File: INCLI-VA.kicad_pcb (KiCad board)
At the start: 2 copper layers, 100 x 100 mm, 168 parts, among them J1 MSTBV 2,5/5-GF-5,08, J2 MSTBV 2,5/2-GF-5,08, J401 USB4105-GF-A, J402 UART0, Q101 STD18NF25, Q102 IPD30N10S3L-34, Q701 DMN10H220LQ, Q751 DMN10H220LQ, SW401 RESET, SW402 BOOT, U101 LM74930QRGERQ1, U201 LMR38010SQDDARQ1, U301 TPS62A02QDRLRQ1, U302 LP5907QMFX-3.3Q1, U401 ESP32-S3-WROOM-1-N8R2, U402 USBLC6-2SC6, U501 SCL3300-D01, U502 ASM330LHHTR, U503 AS5147U-HTSM, U601 ADM3055E, U701 74AHCT1G126, U751 74AHCT1G126, U801 TPS3828-33Q1

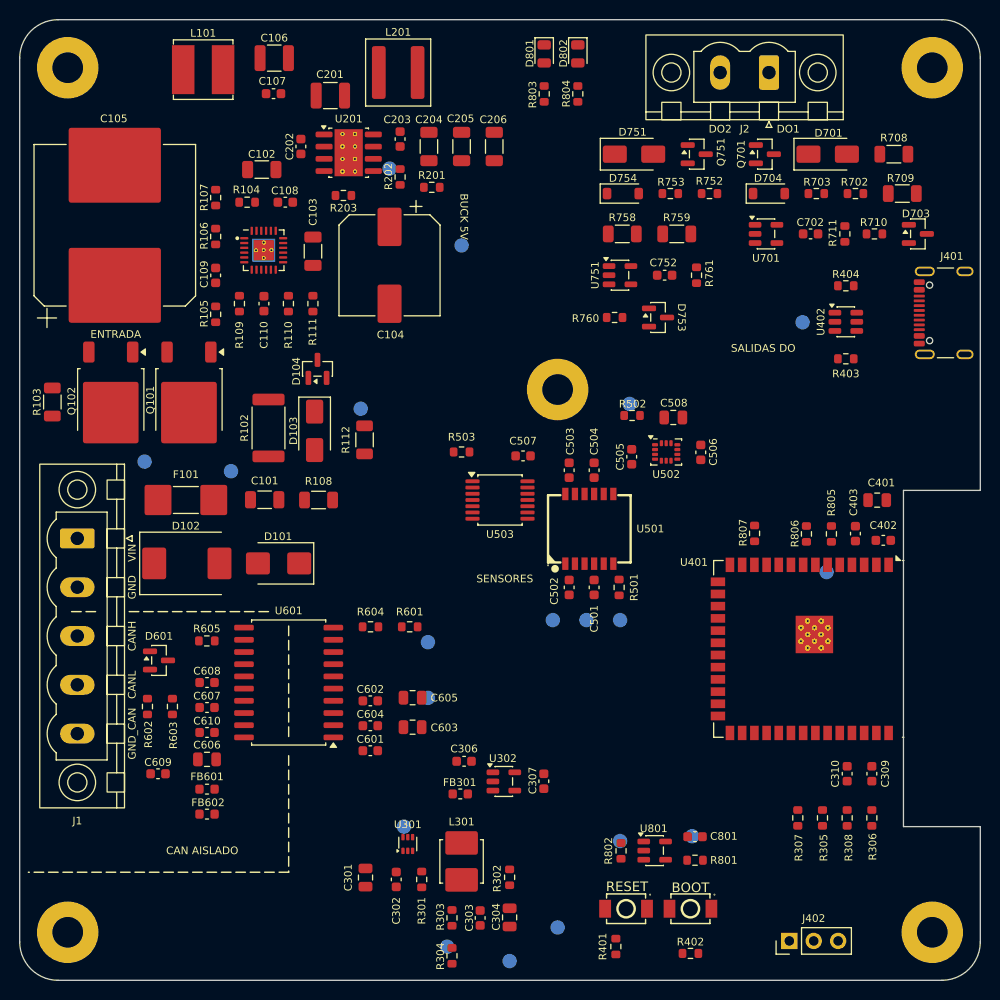
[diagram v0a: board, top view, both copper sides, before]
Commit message: [Claude Code] PCB: placement-v1 - desacoples de U601, lazo del buck, C105 J16 Panasonic y zonas sin barniz
- C601 a 1.1 mm del pin VIO (ADI Rev. D: pista <= 2 mm); C604, C607/C608 reordenados.
- L201 y C203 mas cerca de U201 (SW 2.8 mm, BOOT 1.1 mm).
- C105: huella INCLI-VA:CP_Elec_Panasonic_J16_VibProof (land antivibracion J16, acepta
  EEE-FK1H102AV y EEE-FK1H102AM); MPN PROD EEE-FK1H102AV.
- Coating: zonas a enmascarar en User.Comments y rotulo "SIN BARNIZ".
- PENDIENTES: decisiones del usuario cerradas, requisitos de la caja y plan de ruteo.
- DRC 0 errores, paridad 0. ERC sin cambios.

Co-Authored-By: Claude Opus 5.5 <noreply@anthropic.com>
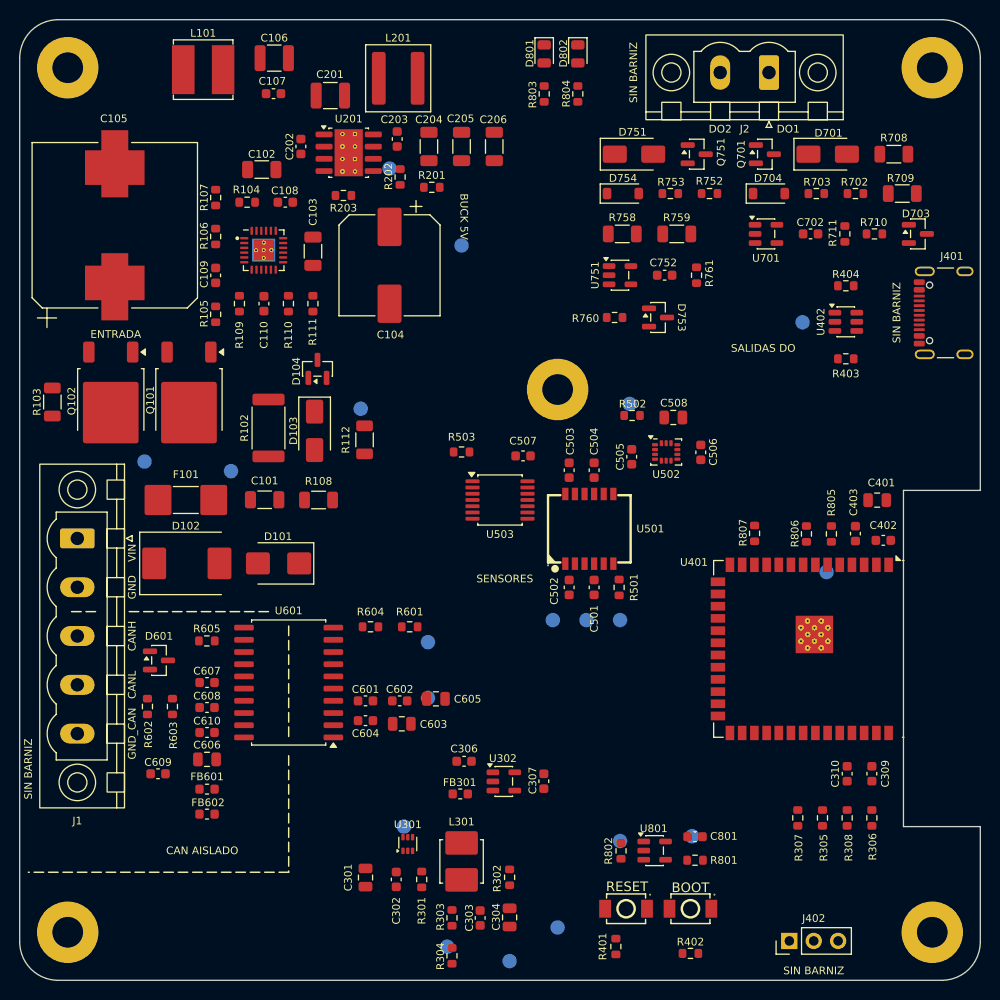
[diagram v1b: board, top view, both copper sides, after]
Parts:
- C105: footprint Capacitor_SMD:CP_Elec_16x17.5 -> INCLI-VA:CP_Elec_Panasonic_J16_VibProof
- moved C601 5.21 mm to (136.0, 120.9)
- moved C602 3.06 mm to (139.6, 120.9)
- moved C607 2.60 mm to (119.5, 119.0)
- moved C608 2.60 mm to (119.5, 121.6)
- moved C605 2.43 mm to (143.3, 120.7)
- moved C603 1.17 mm to (139.8, 123.3)
- moved C604 0.73 mm to (136.0, 123.0)
- moved L201 0.60 mm to (139.4, 56.1)
- moved C203 0.30 mm to (139.3, 62.4)
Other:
- board text added: "SIN BARNIZ"

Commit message: [Claude Code] ruteo etapa 1: potencia (entrada, FETs, Kelvin R103, buck U201, +5V, U301, U302)
- Entrada y protección en F.Cu de 1.5 mm; VA entre C105 y los gates; VOUT por el borde oeste.
- Kelvin de R103 en dos pistas paralelas hasta U101 (CS+, CS-, ISCP) con arcos en B.Cu.
- U201: SW de 3.7 x 1.2 mm, C202 en VIN, FB alto desde C204, vía a GND en C204-C206.
- +5V hasta FB301/U302 y U301; U301 con VIN/EN/FB cruzando bajo SW por B.Cu.
- C104 pasa a B.Cu debajo de C105 (autorizado por el usuario).
- .kicad_dru: sensado HV (pistas <= 0.3 mm), ZONA_U101 a 0.2 mm, VA-gates (Vgs), C202 en la llegada a U201.
- DRC 0 errores, paridad 0, 291 sin rutear (358 antes).

Co-Authored-By: Claude Opus 5.5 <noreply@anthropic.com>
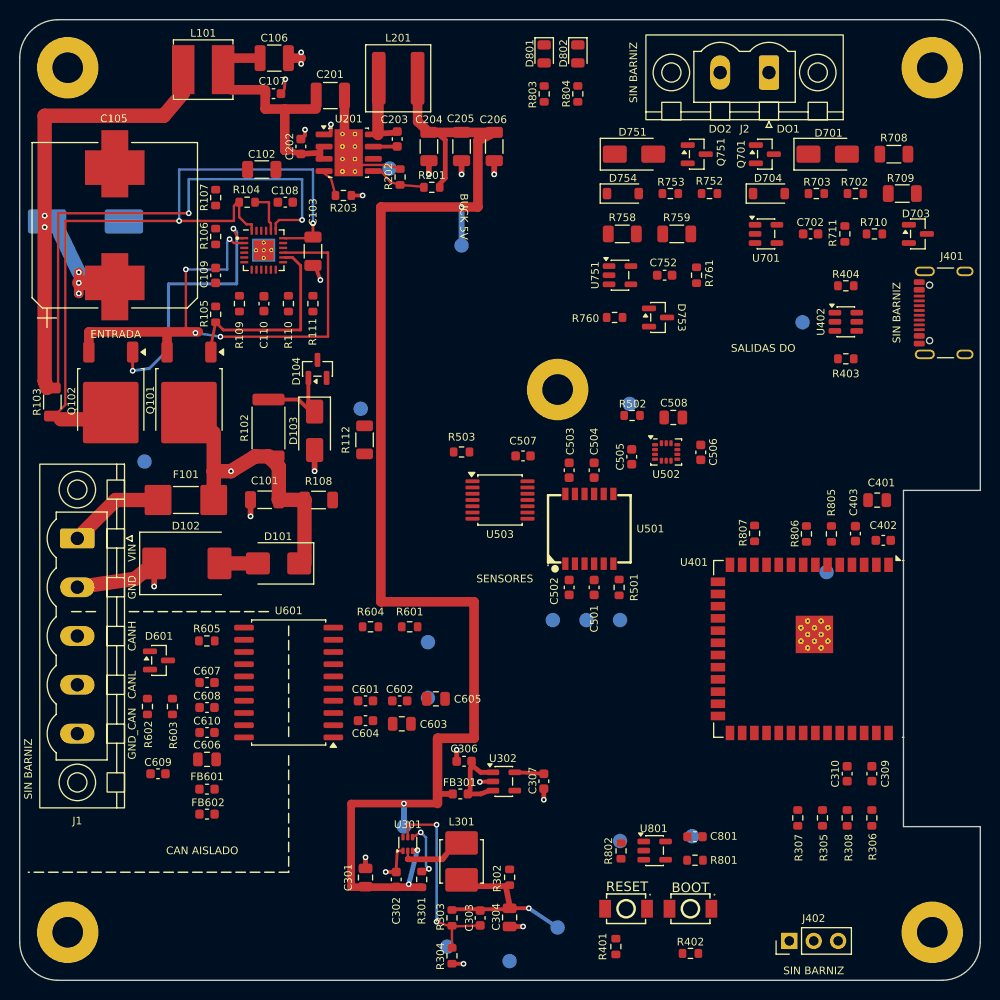
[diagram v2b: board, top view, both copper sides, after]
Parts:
- C104: moved to B.Cu
- moved C104 32.0 mm to (106.8, 71.0), turned to 0 degrees
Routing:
- net +5V_VEH: track 0.00 -> 147.4 mm, vias 0 -> 4
- net /10_power_input/VOUT: track 0.00 -> 109.0 mm, vias 0 -> 7
- net /10_power_input/C_ID: track 0.00 -> 75.1 mm, vias 0 -> 2
- net /10_power_input/VA: track 0.00 -> 58.2 mm, vias 0 -> 4
- net GND_VEH: track 0.00 -> 40.3 mm, vias 0 -> 20
- net /10_power_input/DGATE: track 0.00 -> 27.9 mm, vias 0 -> 2
- net /10_power_input/VBAT_F: track 0.00 -> 27.4 mm, vias 0 -> 1
- net +VPROT: track 0.00 -> 22.6 mm
- net Net-(U301-FB): track 0.00 -> 20.7 mm, vias 0 -> 2
- net /10_power_input/HGATE: track 0.00 -> 20.4 mm
- net +3V3_D: track 0.00 -> 15.9 mm, vias 0 -> 1
- net /10_power_input/VIN_VEH: track 0.00 -> 10.1 mm
- net Net-(U302-EN): track 0.00 -> 7.06 mm
- net Net-(U301-EN): track 0.00 -> 5.80 mm, vias 0 -> 2
- net /20_buck_5v/BUCK_SW: track 0.00 -> 5.45 mm
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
